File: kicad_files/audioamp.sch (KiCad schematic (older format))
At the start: 26 parts

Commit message: Amplificador conectado - Não verificado
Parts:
- added J2: Conn_01x02_Female, symbol Connector:Conn_01x02_Female
- gave numbers to parts that had none: 26
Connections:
- net +VDC: now also C4.1, C6.1, D1.1 (K), D4.1 (K), U1.5 (+Vs), U2.5 (+Vs)
- net -VDC: now also C3.1, C8.1, D2.2 (A), D3.2 (A), U1.3 (-Vs), U2.3 (-Vs)
- net GND: now also C3.2, C4.2, C6.2, C8.2, R1.2, R2.2, R4.2, R5.2, R8.2, R9.2, J2.1 (Pin_1)
- net at U1.1 (+): now also C1.2, R1.1
- net at U1.2 (-): now also C2.1, R3.2
- net at U1.4: now also C5.1, D1.2 (A), D2.1 (K), LS1.1, R3.1, R7.2
- net at U2.1 (+): now also R9.1
- net at U2.2 (-): now also C9.1, R6.2
- net at U2.4: now also C7.1, D3.1 (K), D4.2 (A), LS1.2, R6.1
- net +SIG_F: now reaches C1.1
- net at C2.2: now also R2.1
- net at C9.2: now also R7.1, R8.1
- net at C5.2: now also R4.1
- net at C7.2: now also R5.1
- new net +SIG: J2.2 (Pin_2)
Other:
- moved on the sheet: C1, C2, C3, C4, C5, C6, C7, C8, C9, D1, D2, D3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

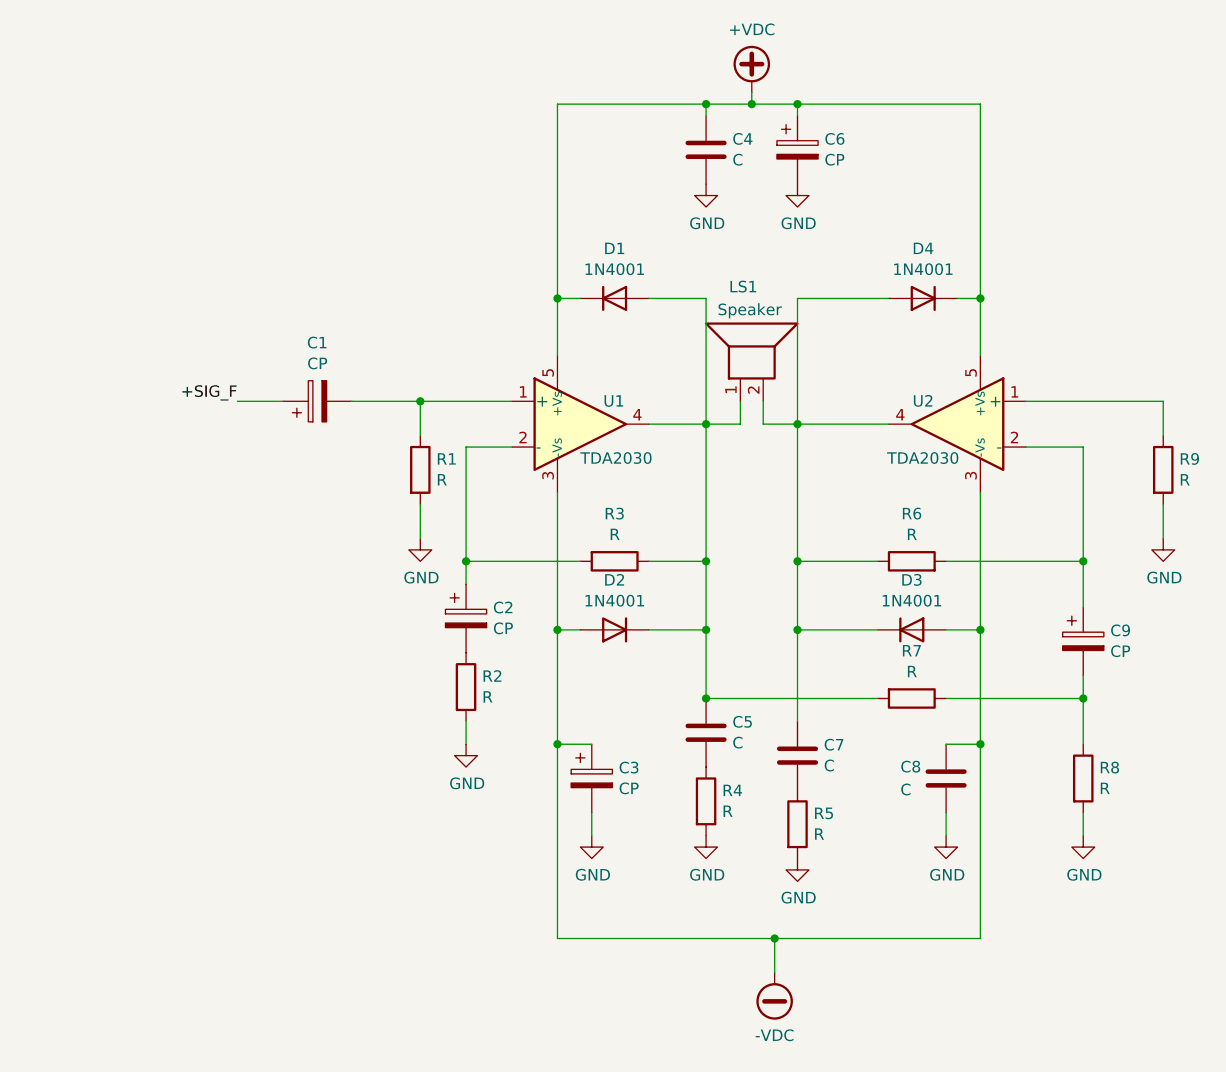
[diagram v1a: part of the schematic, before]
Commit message: Adicionados valores do amplificador - Verificado
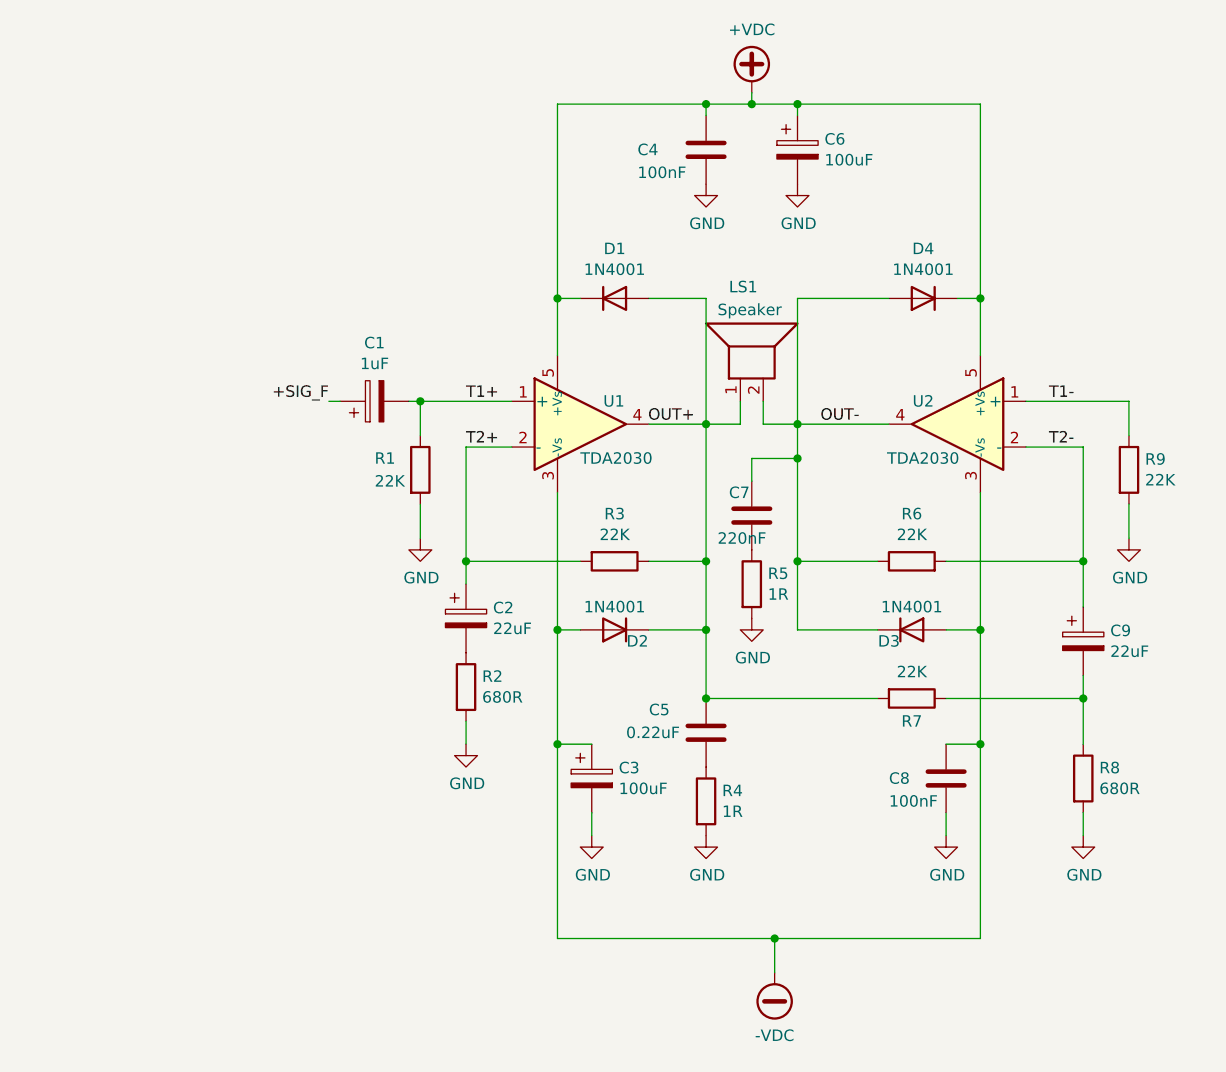
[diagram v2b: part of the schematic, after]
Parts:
- C1: value CP -> 1uF
- C2, C9: value CP -> 22uF
- C3, C6: value CP -> 100uF
- C4, C8: value C -> 100nF
- C5: value C -> 0.22uF
- C7: value C -> 220nF
- R1, R3, R6, R7, R9: value R -> 22K
- R2, R8: value R -> 680R
- R4, R5: value R -> 1R
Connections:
- net T1+: now reaches C1.2, R1.1, U1.1 (+)
- net T2+: now reaches C2.1, R3.2, U1.2 (-)
- net OUT+: now reaches C5.1, D1.2 (A), D2.1 (K), LS1.1, R3.1, R7.2, U1.4
- net T1-: now reaches R9.1, U2.1 (+)
- net T2-: now reaches C9.1, R6.2, U2.2 (-)
- net OUT-: now reaches C7.1, D3.1 (K), D4.2 (A), LS1.2, R6.1, U2.4
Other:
- moved on the sheet: C1, C7, R5, R9
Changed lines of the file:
@@
 P 8000 3900
 F 0 "C3" H 8118 3946 50  0000 L CNN
-F 1 "CP" H 8118 3855 50  0000 L CNN
+F 1 "100uF" H 8118 3855 50  0000 L CNN
 F 2 "" H 8038 3750 50  0001 C CNN
 F 3 "~" H 8000 3900 50  0001 C CNN
@@
 L Device:CP C1
 U 1 1 5EFBE772
-P 6800 2250
-F 0 "C1" V 7055 2250 50  0000 C CNN
-F 1 "CP" V 6964 2250 50  0000 C CNN
-F 2 "" H 6838 2100 50  0001 C CNN
-F 3 "~" H 6800 2250 50  0001 C CNN
-	1    6800 2250
+P 7050 2250
+F 0 "C1" V 7305 2250 50  0000 C CNN
+F 1 "1uF" V 7214 2250 50  0000 C CNN
+F 2 "" H 7088 2100 50  0001 C CNN
+F 3 "~" H 7050 2250 50  0001 C CNN
+	1    7050 2250
 	0    -1   -1   0
 $EndComp
@@
 P 7450 3200
 F 0 "C2" H 7568 3246 50  0000 L CNN
-F 1 "CP" H 7568 3155 50  0000 L CNN
+F 1 "22uF" H 7568 3155 50  0000 L CNN
 F 2 "" H 7488 3050 50  0001 C CNN
 F 3 "~" H 7450 3200 50  0001 C CNN
@@
 P 10150 3300
 F 0 "C9" H 10268 3346 50  0000 L CNN
-F 1 "CP" H 10268 3255 50  0000 L CNN
+F 1 "22uF" H 10268 3255 50  0000 L CNN
 F 2 "" H 10188 3150 50  0001 C CNN
 F 3 "~" H 10150 3300 50  0001 C CNN
@@
 P 8900 1150
 F 0 "C6" H 9018 1196 50  0000 L CNN
-F 1 "CP" H 9018 1105 50  0000 L CNN
+F 1 "100uF" H 9018 1105 50  0000 L CNN
 F 2 "" H 8938 1000 50  0001 C CNN
 F 3 "~" H 8900 1150 50  0001 C CNN
@@
 U 1 1 5EFC068C
 P 8500 3700
-F 0 "C5" H 8615 3746 50  0000 L CNN
-F 1 "C" H 8615 3655 50  0000 L CNN
+F 0 "C5" H 8250 3800 50  0000 L CNN
+F 1 "0.22uF" H 8150 3700 50  0000 L CNN
 F 2 "" H 8538 3550 50  0001 C CNN
 F 3 "~" H 8500 3700 50  0001 C CNN
@@
 U 1 1 5EFC0A87
 P 8500 1150
-F 0 "C4" H 8615 1196 50  0000 L CNN
-F 1 "C" H 8615 1105 50  0000 L CNN
+F 0 "C4" H 8200 1150 50  0000 L CNN
+F 1 "100nF" H 8200 1050 50  0000 L CNN
 F 2 "" H 8538 1000 50  0001 C CNN
 F 3 "~" H 8500 1150 50  0001 C CNN
@@
 L Device:C C7
 U 1 1 5EFC0EC5
-P 8900 3800
-F 0 "C7" H 9015 3846 50  0000 L CNN
-F 1 "C" H 9015 3755 50  0000 L CNN
-F 2 "" H 8938 3650 50  0001 C CNN
-F 3 "~" H 8900 3800 50  0001 C CNN
-	1    8900 3800
+P 8700 2750
+F 0 "C7" H 8600 2850 50  0000 L CNN
+F 1 "220nF" H 8550 2650 50  0000 L CNN
+F 2 "" H 8738 2600 50  0001 C CNN
+F 3 "~" H 8700 2750 50  0001 C CNN
+	1    8700 2750
 	1    0    0    -1
 $EndComp
@@
 U 1 1 5EFC1365
 P 9550 3900
-F 0 "C8" H 9350 3950 50  0000 L CNN
-F 1 "C" H 9350 3850 50  0000 L CNN
+F 0 "C8" H 9300 3900 50  0000 L CNN
+F 1 "100nF" H 9300 3800 50  0000 L CNN
 F 2 "" H 9588 3750 50  0001 C CNN
 F 3 "~" H 9550 3900 50  0001 C CNN
@@
 U 1 1 5EFC2137
 P 7250 2550
-F 0 "R1" H 7320 2596 50  0000 L CNN
-F 1 "R" H 7320 2505 50  0000 L CNN
+F 0 "R1" H 7050 2600 50  0000 L CNN
+F 1 "22K" H 7050 2500 50  0000 L CNN
 F 2 "" V 7180 2550 50  0001 C CNN
 F 3 "~" H 7250 2550 50  0001 C CNN
@@
 P 8100 2950
 F 0 "R3" V 7893 2950 50  0000 C CNN
-F 1 "R" V 7984 2950 50  0000 C CNN
+F 1 "22K" V 7984 2950 50  0000 C CNN
 F 2 "" V 8030 2950 50  0001 C CNN
 F 3 "~" H 8100 2950 50  0001 C CNN
@@
 P 7450 3500
 F 0 "R2" H 7520 3546 50  0000 L CNN
-F 1 "R" H 7520 3455 50  0000 L CNN
+F 1 "680R" H 7520 3455 50  0000 L CNN
 F 2 "" V 7380 3500 50  0001 C CNN
 F 3 "~" H 7450 3500 50  0001 C CNN
@@
 L Device:R R9
 U 1 1 5EFC29EB
-P 10500 2550
-F 0 "R9" H 10570 2596 50  0000 L CNN
-F 1 "R" H 10570 2505 50  0000 L CNN
-F 2 "" V 10430 2550 50  0001 C CNN
-F 3 "~" H 10500 2550 50  0001 C CNN
-	1    10500 2550
+P 10350 2550
+F 0 "R9" H 10420 2596 50  0000 L CNN
+F 1 "22K" H 10420 2505 50  0000 L CNN
+F 2 "" V 10280 2550 50  0001 C CNN
+F 3 "~" H 10350 2550 50  0001 C CNN
+	1    10350 2550
 	1    0    0    -1
 $EndComp
@@
 P 10150 3900
 F 0 "R8" H 10220 3946 50  0000 L CNN
-F 1 "R" H 10220 3855 50  0000 L CNN
+F 1 "680R" H 10220 3855 50  0000 L CNN
 F 2 "" V 10080 3900 50  0001 C CNN
 F 3 "~" H 10150 3900 50  0001 C CNN
@@
 U 1 1 5EFC3091
 P 9400 3550
-F 0 "R7" V 9193 3550 50  0000 C CNN
-F 1 "R" V 9284 3550 50  0000 C CNN
+F 0 "R7" V 9500 3550 50  0000 C CNN
+F 1 "22K" V 9284 3550 50  0000 C CNN
 F 2 "" V 9330 3550 50  0001 C CNN
 F 3 "~" H 9400 3550 50  0001 C CNN
@@
 P 9400 2950
 F 0 "R6" V 9607 2950 50  0000 C CNN
-F 1 "R" V 9516 2950 50  0000 C CNN
+F 1 "22K" V 9516 2950 50  0000 C CNN
 F 2 "" V 9330 2950 50  0001 C CNN
 F 3 "~" H 9400 2950 50  0001 C CNN
@@
 P 8500 4000
 F 0 "R4" H 8570 4046 50  0000 L CNN
-F 1 "R" H 8570 3955 50  0000 L CNN
+F 1 "1R" H 8570 3955 50  0000 L CNN
 F 2 "" V 8430 4000 50  0001 C CNN
 F 3 "~" H 8500 4000 50  0001 C CNN
@@
 U 1 1 5EFC5A4E
 P 8100 3250
-F 0 "D2" H 8100 3033 50  0000 C CNN
-F 1 "1N4001" H 8100 3124 50  0000 C CNN
+F 0 "D2" H 8000 3300 50  0000 C CNN
+F 1 "1N4001" H 8100 3150 50  0000 C CNN
 F 2 "Diode_THT:D_DO-41_SOD81_P10.16mm_Horizontal" H 8100 3075 50  0001 C CNN
 F 3 "http://www.vishay.com/docs/88503/1n4001.pdf" H 8100 3250 50  0001 C CNN
 	1    8100 3250
 	-1   0    0    1
-$EndComp
-$Comp
-L Diode:1N4001 D3
-U 1 1 5EFC651D
-P 9400 3250
-F 0 "D3" H 9400 3467 50  0000 C CNN
-F 1 "1N4001" H 9400 3376 50  0000 C CNN
-F 2 "Diode_THT:D_DO-41_SOD81_P10.16mm_Horizontal" H 9400 3075 50  0001 C CNN
-F 3 "http://www.vishay.com/docs/88503/1n4001.pdf" H 9400 3250 50  0001 C CNN
-	1    9400 3250
-	1    0    0    -1
 $EndComp
 $Comp
@@
 	2000 6300 1400 6300
 Wire Wire Line
-	6950 2250 7250 2250
+	7200 2250 7250 2250
 Wire Wire Line
 	7250 2250 7250 2400
@@
 Connection ~ 7250 2250
 Wire Wire Line
-	6650 2250 6450 2250
-Text Label 6450 2250 2    50   ~ 0
+	6900 2250 6850 2250
+Text Label 6850 2250 2    50   ~ 0
 +SIG_F
 $Comp
@@
 	7850 1800 7950 1800
 Wire Wire Line
-	8900 2950 8900 2350
+	8900 2950 8900 2500
 Connection ~ 8900 2350
 Wire Wire Line
@@
 	9700 1800 9600 1800
 Wire Wire Line
-	9900 2250 10500 2250
-Wire Wire Line
-	10500 2250 10500 2400
+	9900 2250 10350 2250
+Wire Wire Line
+	10350 2250 10350 2400
 Wire Wire Line
 	9900 2450 10150 2450
@@
 L power:GND #PWR0106
 U 1 1 5F0025E0
-P 10500 2850
-F 0 "#PWR0106" H 10500 2600 50  0001 C CNN
-F 1 "GND" H 10505 2677 50  0000 C CNN
-F 2 "" H 10500 2850 50  0001 C CNN
-F 3 "" H 10500 2850 50  0001 C CNN
-	1    10500 2850
-	1    0    0    -1
-$EndComp
-Wire Wire Line
-	10500 2700 10500 2850
+P 10350 2850
+F 0 "#PWR0106" H 10350 2600 50  0001 C CNN
+F 1 "GND" H 10355 2677 50  0000 C CNN
+F 2 "" H 10350 2850 50  0001 C CNN
+F 3 "" H 10350 2850 50  0001 C CNN
+	1    10350 2850
+	1    0    0    -1
+$EndComp
+Wire Wire Line
+	10350 2700 10350 2850
 Wire Wire Line
 	10150 3450 10150 3550
@@
 L Device:R R5
 U 1 1 5EFC3390
-P 8900 4100
-F 0 "R5" H 8970 4146 50  0000 L CNN
-F 1 "R" H 8970 4055 50  0000 L CNN
-F 2 "" V 8830 4100 50  0001 C CNN
-F 3 "~" H 8900 4100 50  0001 C CNN
-	1    8900 4100
+P 8700 3050
+F 0 "R5" H 8770 3096 50  0000 L CNN
+F 1 "1R" H 8770 3005 50  0000 L CNN
+F 2 "" V 8630 3050 50  0001 C CNN
+F 3 "~" H 8700 3050 50  0001 C CNN
+	1    8700 3050
 	1    0    0    -1
 $EndComp
@@
 L power:GND #PWR0112
 U 1 1 5F0228E4
-P 8900 4250
-F 0 "#PWR0112" H 8900 4000 50  0001 C CNN
-F 1 "GND" H 8905 4077 50  0000 C CNN
-F 2 "" H 8900 4250 50  0001 C CNN
-F 3 "" H 8900 4250 50  0001 C CNN
-	1    8900 4250
+P 8700 3200
+F 0 "#PWR0112" H 8700 2950 50  0001 C CNN
+F 1 "GND" H 8705 3027 50  0000 C CNN
+F 2 "" H 8700 3200 50  0001 C CNN
+F 3 "" H 8700 3200 50  0001 C CNN
+	1    8700 3200
 	1    0    0    -1
 $EndComp
@@
 	8900 3250 8900 2950
 Connection ~ 8900 2950
-Wire Wire Line
-	8900 3250 8900 3650
-Connection ~ 8900 3250
 Wire Wire Line
 	7850 3750 7850 4600
@@
 	0    -1   -1   0
 $EndComp
+$Comp
+L Diode:1N4001 D3
+U 1 1 5EFC651D
+P 9400 3250
+F 0 "D3" H 9300 3200 50  0000 C CNN
+F 1 "1N4001" H 9400 3350 50  0000 C CNN
+F 2 "Diode_THT:D_DO-41_SOD81_P10.16mm_Horizontal" H 9400 3075 50  0001 C CNN
+F 3 "http://www.vishay.com/docs/88503/1n4001.pdf" H 9400 3250 50  0001 C CNN
+	1    9400 3250
+	1    0    0    -1
+$EndComp
+Wire Wire Line
+	8700 2600 8700 2500
+Wire Wire Line
+	8700 2500 8900 2500
+Connection ~ 8900 2500
+Wire Wire Line
+	8900 2500 8900 2350
+Text Label 8450 2350 2    50   ~ 0
+OUT+
+Text Label 9000 2350 0    50   ~ 0
+OUT-
+Text Label 7450 2250 0    50   ~ 0
+T1+
+Text Label 7450 2450 0    50   ~ 0
+T2+
+Text Label 10000 2250 0    50   ~ 0
+T1-
+Text Label 10000 2450 0    50   ~ 0
+T2-
 $EndSCHEMATC
